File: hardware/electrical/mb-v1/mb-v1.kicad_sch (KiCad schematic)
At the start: 17 parts, among them SW1 SW_MEC_5E, SW2 SW_MEC_5E, SW3 SW_MEC_5E, SW5 SW_MEC_5E, U1 ATmega328P-A, U2 PCF8574T, Y1 Crystal_GND24

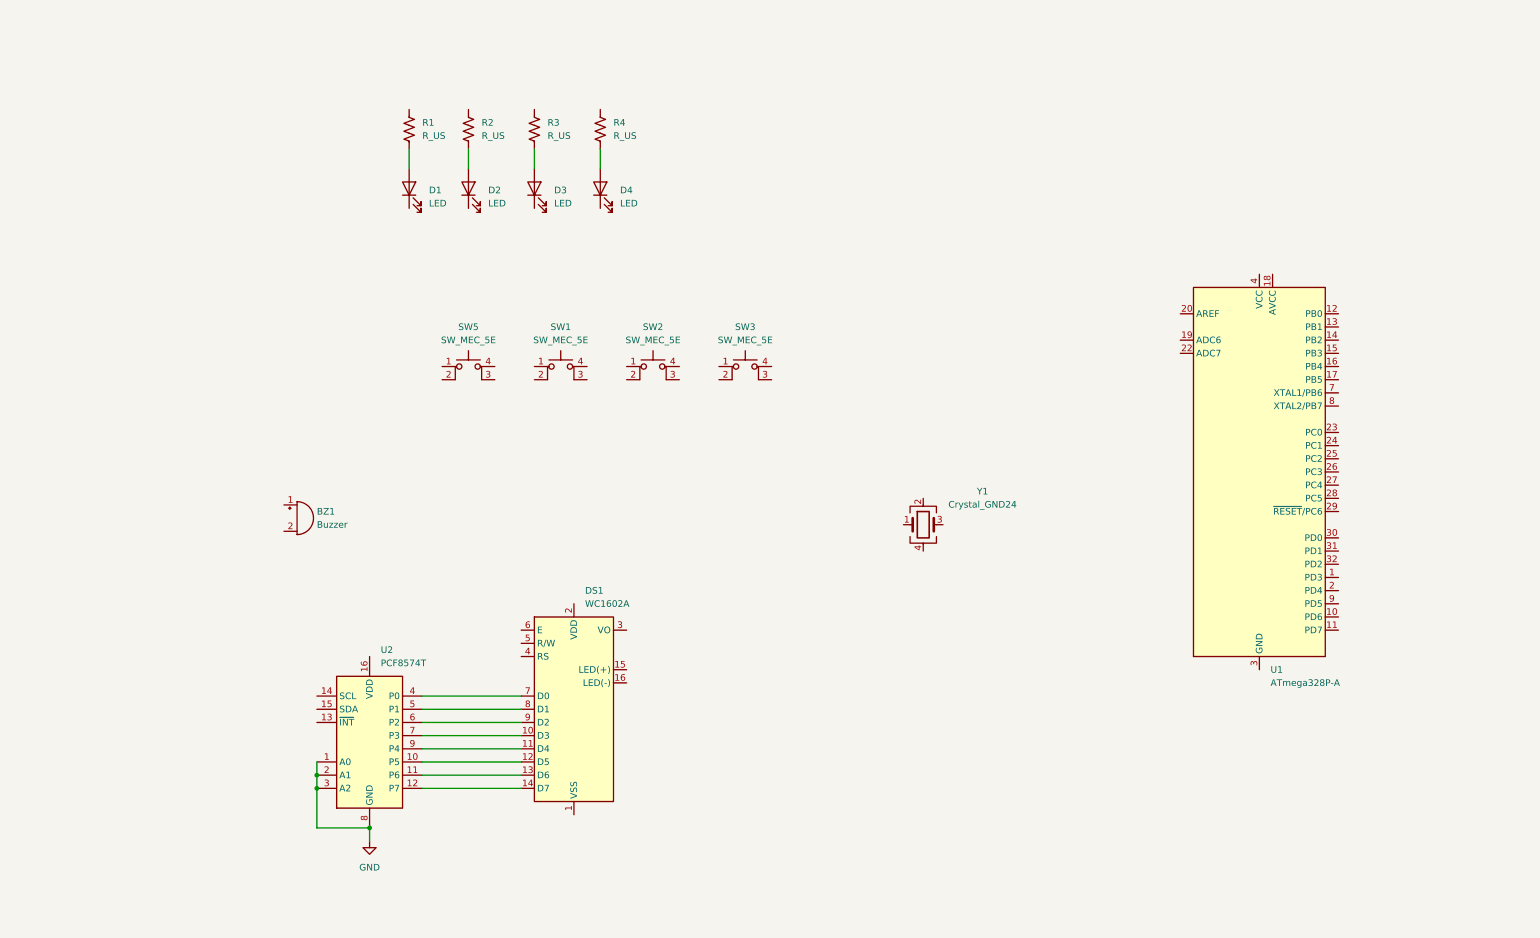
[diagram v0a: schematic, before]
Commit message: organize leds, buttons and buzzer
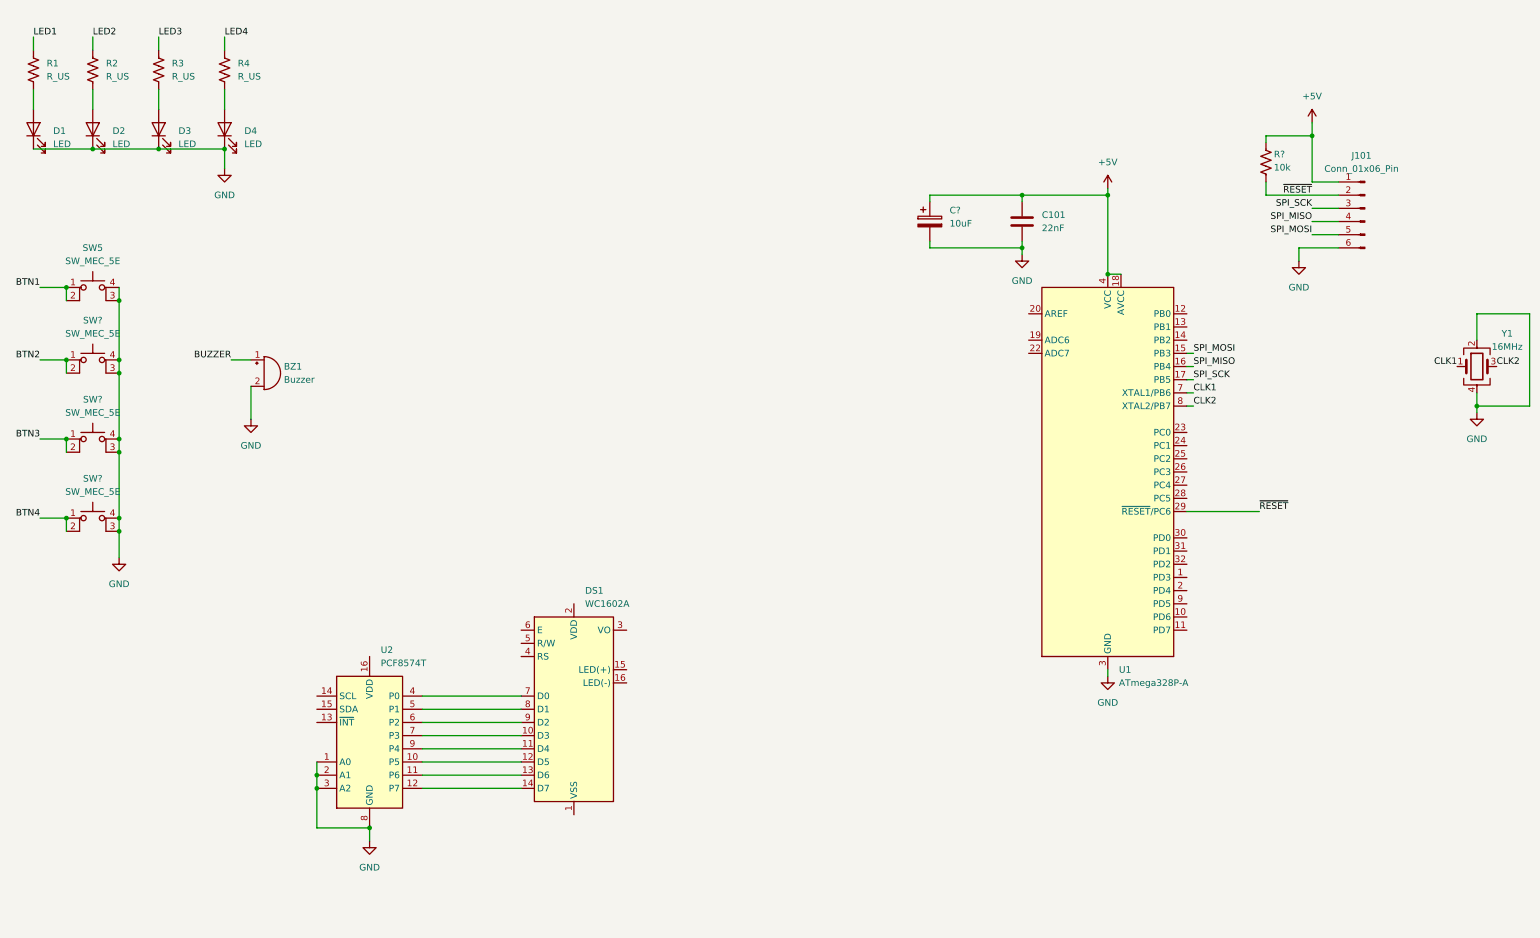
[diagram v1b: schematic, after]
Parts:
- removed SW1, SW2, SW3: SW_MEC_5E, symbol Switch:SW_MEC_5E
- added C101: 22nF, symbol Device:C
- added C?: 10uF, symbol Device:C_Polarized
- added J101: Conn_01x06_Pin, symbol Connector:Conn_01x06_Pin
- added R?: 10k, symbol Device:R_US
- added SW? (x3): SW_MEC_5E, symbol Switch:SW_MEC_5E
- Y1: value Crystal_GND24 -> 16MHz
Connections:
- net GND: now also BZ1.2 (-), D1.1 (K), D2.1 (K), D3.1 (K), D4.1 (K), SW5.3 (K), SW5.4 (A), U1.21 (GND), U1.3 (GND), U1.5 (GND), Y1.2, Y1.4, C101.2, C?.2, J101.6 (Pin_6), SW?.3 (K), SW?.3 (K), SW?.3 (K), SW?.4 (A), SW?.4 (A), SW?.4 (A)
- net SPI_MOSI: now reaches U1.15 (PB3)
- net SPI_MOSI: now also J101.5 (Pin_5)
- net SPI_MISO: now reaches U1.16 (PB4)
- net SPI_MISO: now also J101.4 (Pin_4)
- net SPI_SCK: now reaches U1.17 (PB5)
- net SPI_SCK: now also J101.3 (Pin_3)
- net +5V: now reaches U1.18 (AVCC)
- net +5V: now also U1.4 (VCC), U1.6 (VCC), C101.1, C?.1, J101.1 (Pin_1), R?.1
- net ~{RESET}: now reaches U1.29 (~{RESET}/PC6)
- net ~{RESET}: now also J101.2 (Pin_2), R?.2
- net CLK1: now reaches U1.7 (XTAL1/PB6)
- net CLK1: now also Y1.1
- net CLK2: now reaches U1.8 (XTAL2/PB7)
- net CLK2: now also Y1.3
- net LED1: now reaches R1.1
- net BUZZER: now reaches BZ1.1 (+)
- net LED4: now reaches R4.1
- net BTN1: now reaches SW5.1
- net BTN1: now also SW5.2
- net LED2: now reaches R2.1
- net LED3: now reaches R3.1
- new net BTN2: SW?.1, SW?.2
- new net BTN3: SW?.1, SW?.2
- new net BTN4: SW?.1, SW?.2
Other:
- moved on the sheet: BZ1, D1, D2, D3, D4, R1, R2, R3, R4, SW5, U1, Y1

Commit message: add usb and usb-serial converter
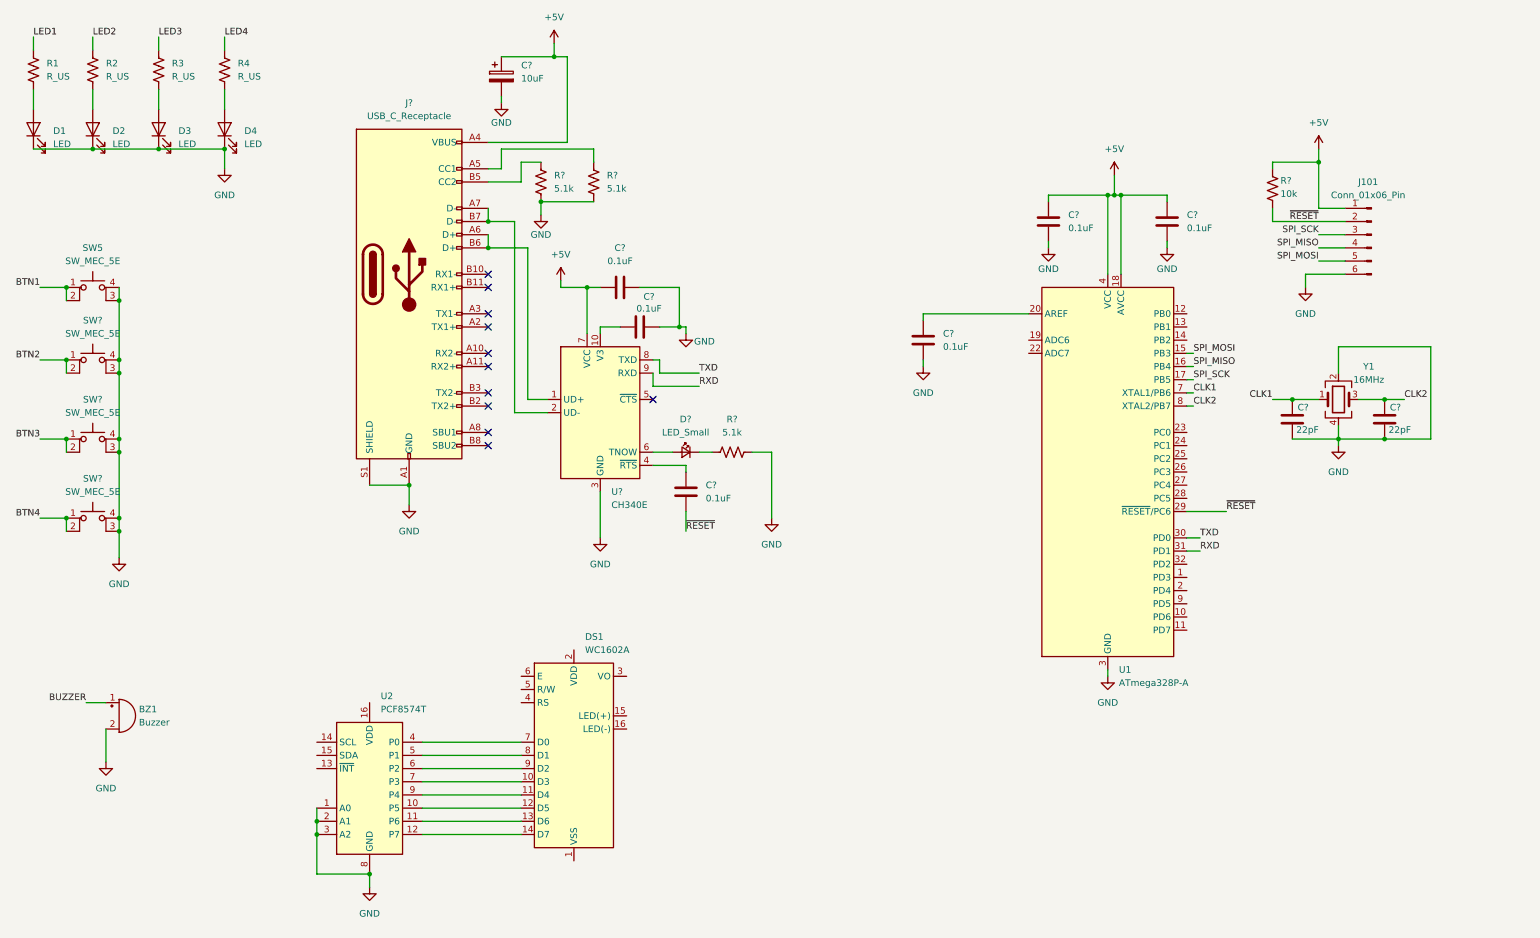
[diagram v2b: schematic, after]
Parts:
- removed C101: 22nF, symbol Device:C
- added C? (x2): 22pF, symbol Device:C
- added C? (x6): 0.1uF, symbol Device:C
- added D?: LED_Small, symbol Device:LED_Small
- added J?: USB_C_Receptacle, symbol Connector:USB_C_Receptacle
- added R? (x3): 5.1k, symbol Device:R_US
- added U?: CH340E, Package_SO:MSOP-10_3x3mm_P0.5mm, symbol Interface_USB:CH340E
- Y1: footprint (none) -> Crystal:Crystal_SMD_SeikoEpson_TSX3225-4Pin_3.2x2.5mm
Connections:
- net +5V: now also C?.1, C?.1, C?.1, J?.A4 (VBUS), J?.A9 (VBUS), J?.B4 (VBUS), J?.B9 (VBUS), U?.7 (VCC)
- net CLK1: now also C?.1
- net CLK2: now also C?.1
- net GND: now also C?.2, C?.2, C?.2, C?.2, C?.2, C?.2, C?.2, J?.A1 (GND), J?.A12 (GND), J?.B1 (GND), J?.B12 (GND), J?.S1 (SHIELD), R?.2, R?.2, R?.2, U?.3 (GND)
- net ~{RESET}: now also C?.2
- net at U1.20 (AREF): now also C?.1
- net TXD: now reaches U1.30 (PD0)
- net TXD: now also U?.8 (TXD)
- net RXD: now reaches U1.31 (PD1)
- net RXD: now also U?.9 (RXD)
- new net: J?.A6 (D+), J?.B6 (D+), U?.1 (UD+)
- new net: C?.1, U?.10 (V3)
- new net: J?.A7 (D-), J?.B7 (D-), U?.2 (UD-)
- new net: C?.1, U?.4 (~{RTS})
- new net: D?.2 (A), U?.6 (TNOW)
- new net: J?.A5 (CC1), R?.1
- new net: J?.B5 (CC2), R?.1
- new net: D?.1 (K), R?.1
- no-connect marks 0 -> 11
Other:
- moved on the sheet: BZ1, C?, DS1, J101, R?, U2, Y1

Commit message: complete placement and primary routing
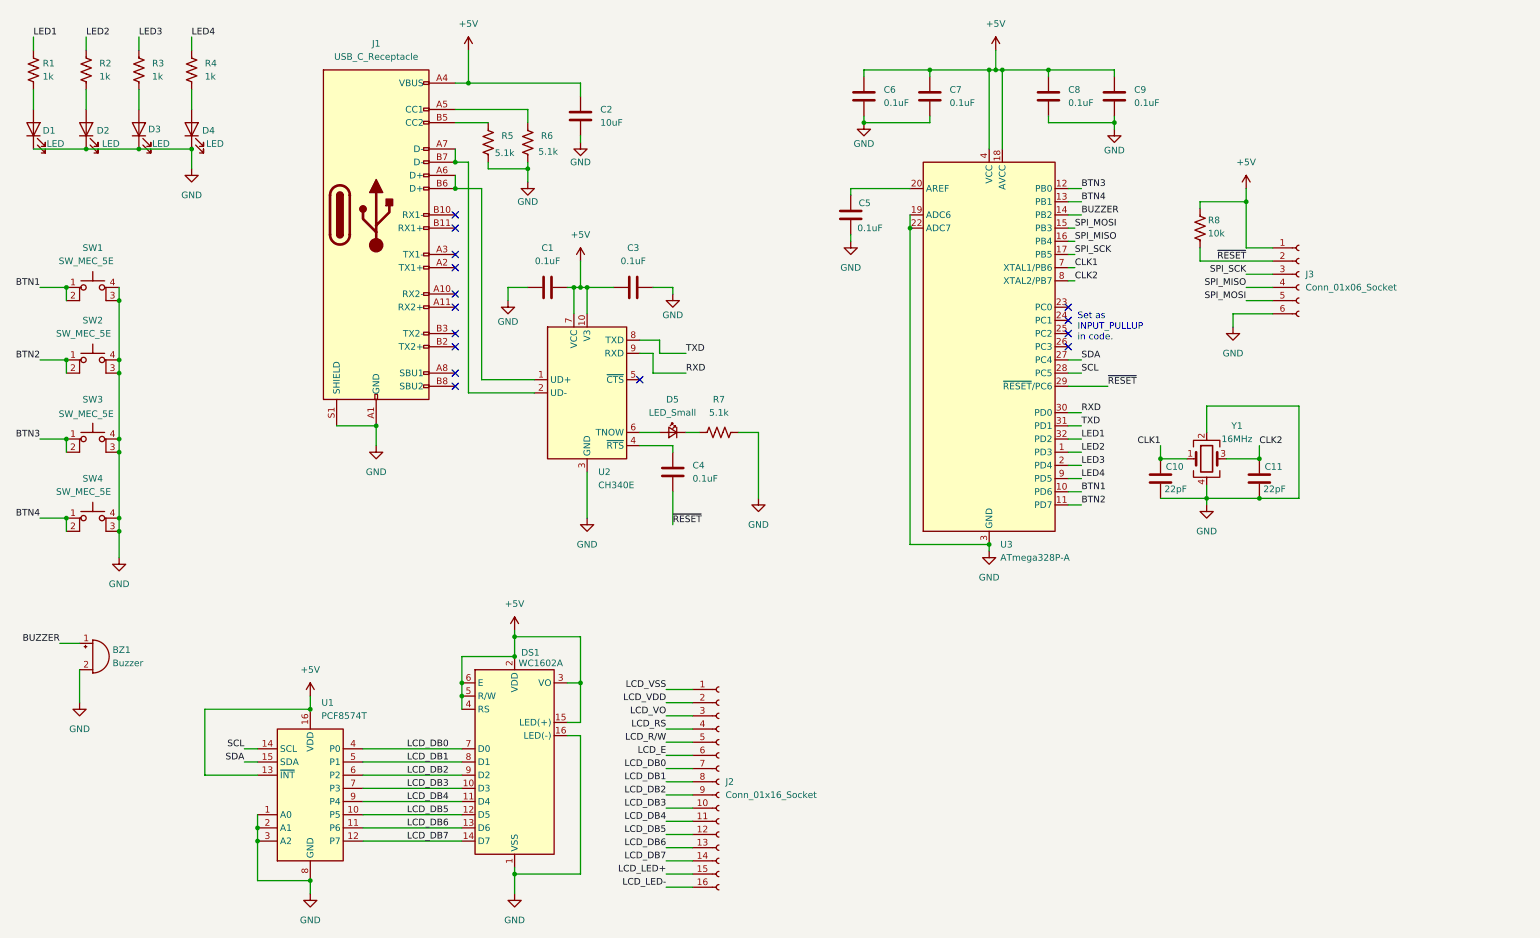
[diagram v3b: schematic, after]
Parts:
- removed C? (x2): 0.1uF, symbol Device:C
- removed C?: 10uF, symbol Device:C_Polarized
- removed J101: Conn_01x06_Pin, symbol Connector:Conn_01x06_Pin
- added C1, C3, C6, C9: 0.1uF, Capacitor_SMD:C_0603_1608Metric, symbol Device:C
- added C2: 10uF, Capacitor_SMD:C_0805_2012Metric, symbol Device:C
- added J2: Conn_01x16_Socket, symbol Connector:Conn_01x16_Socket
- added J3: Conn_01x06_Socket, symbol Connector:Conn_01x06_Socket
- C10, C11: renamed from C?; footprint (none) -> Capacitor_SMD:C_0402_1005Metric
- C4, C5, C7, C8: renamed from C?; footprint (none) -> Capacitor_SMD:C_0603_1608Metric
- J1: renamed from J?; footprint (none) -> Connector_USB:USB_C_Receptacle_Amphenol_12401548E4-2A
- R1, R2, R3, R4: value R_US -> 1k; footprint (none) -> Resistor_SMD:R_0603_1608Metric
- R5, R6, R7, R8: renamed from R?; footprint (none) -> Resistor_SMD:R_0603_1608Metric
- gave numbers to parts that had none: 5
- renumbered SW5 to SW1, U2 to U1, U1 to U3
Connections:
- net +5V: now also DS1.15 (LED(+)), DS1.2 (VDD), DS1.3 (VO), DS1.4 (RS), DS1.5 (R/W), DS1.6 (E), U1.13 (~{INT}), U1.16 (VDD), U2.10 (V3), C1.1, C2.1, C3.1, C6.1, C9.1, J3.1 (Pin_1)
- net BTN1: now also U3.10 (PD6)
- net BTN2: now also U3.11 (PD7)
- net BTN3: now also U3.12 (PB0)
- net BTN4: now also U3.13 (PB1)
- net BUZZER: now also U3.14 (PB2)
- net GND: now also DS1.1 (VSS), DS1.16 (LED(-)), U3.19 (ADC6), U3.22 (ADC7), C1.2, C2.2, C3.2, C6.2, C9.2, J3.6 (Pin_6)
- net LED1: now also U3.32 (PD2)
- net LED2: now also U3.1 (PD3)
- net LED3: now also U3.2 (PD4)
- net LED4: now also U3.9 (PD5)
- net RXD: now also U3.30 (PD0); no longer U3.31 (PD1)
- net SPI_MISO: now also J3.4 (Pin_4)
- net SPI_MOSI: now also J3.5 (Pin_5)
- net SPI_SCK: now also J3.3 (Pin_3)
- net TXD: now also U3.31 (PD1); no longer U3.30 (PD0)
- net ~{RESET}: now also J3.2 (Pin_2)
- net SDA: now reaches U3.27 (PC4)
- net SDA: now also U1.15 (SDA)
- net SCL: now reaches U3.28 (PC5)
- net SCL: now also U1.14 (SCL)
- net LCD_DB5: now reaches DS1.12 (D5), U1.10 (P5)
- net LCD_DB5: now also J2.12 (Pin_12)
- net LCD_DB6: now reaches DS1.13 (D6), U1.11 (P6)
- net LCD_DB6: now also J2.13 (Pin_13)
- net LCD_DB7: now reaches DS1.14 (D7), U1.12 (P7)
- net LCD_DB7: now also J2.14 (Pin_14)
- net LCD_DB0: now reaches DS1.7 (D0), U1.4 (P0)
- net LCD_DB0: now also J2.7 (Pin_7)
- net LCD_DB1: now reaches DS1.8 (D1), U1.5 (P1)
- net LCD_DB1: now also J2.8 (Pin_8)
- net LCD_DB2: now reaches DS1.9 (D2), U1.6 (P2)
- net LCD_DB2: now also J2.9 (Pin_9)
- net LCD_DB3: now reaches DS1.10 (D3), U1.7 (P3)
- net LCD_DB3: now also J2.10 (Pin_10)
- net LCD_DB4: now reaches DS1.11 (D4), U1.9 (P4)
- net LCD_DB4: now also J2.11 (Pin_11)
- new net LCD_E: J2.6 (Pin_6)
- new net LCD_LED+: J2.15 (Pin_15)
- new net LCD_LED-: J2.16 (Pin_16)
- new net LCD_RS: J2.4 (Pin_4)
- new net LCD_R/W: J2.5 (Pin_5)
- new net LCD_VDD: J2.2 (Pin_2)
- new net LCD_VO: J2.3 (Pin_3)
- new net LCD_VSS: J2.1 (Pin_1)
- no-connect marks 11 -> 15
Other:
- note added: "Set as INPUT_PULLUP in code."
- moved on the sheet: BZ1, C10, C11, C4, C5, C7, C8, D2, D3, D4, D5, DS1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

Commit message: replace usb symbol in schematic
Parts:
- added J?: TYPE-C-31-M-12, TYPE-C-31-M-12:HRO_TYPE-C-31-M-12, symbol TYPE-C-31-M-12:TYPE-C-31-M-12
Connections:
- net GND: now also J?.A1_B12 (GND), J?.B1_A12 (GND)
- new net: J?.S1 (SHIELD), J?.S2 (SHIELD), J?.S3 (SHIELD), J?.S4 (SHIELD)
- new net VBUS: J?.A4_B9 (VBUS), J?.B4_A9 (VBUS)
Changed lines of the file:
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@@
+	)
+	(symbol
+		(lib_id "TYPE-C-31-M-12:TYPE-C-31-M-12")
+		(at 77.47 125.73 0)
+		(unit 1)
+		(exclude_from_sim no)
+		(in_bom yes)
+		(on_board yes)
+		(dnp no)
+		(fields_autoplaced yes)
+		(property "Reference" "J?"
+			(at 77.47 107.95 0)
+			(effects
+				(font
+					(size 1.27 1.27)
+				)
+			)
+		)
+		(property "Value" "TYPE-C-31-M-12"
+			(at 77.47 110.49 0)
+			(effects
+				(font
+					(size 1.27 1.27)
+				)
+			)
+		)
+		(property "Footprint" "TYPE-C-31-M-12:HRO_TYPE-C-31-M-12"
+			(at 77.47 125.73 0)
+			(effects
+				(font
+					(size 1.27 1.27)
+				)
+				(justify bottom)
+				(hide yes)
+			)
+		)
+		(property "Datasheet" ""
+			(at 77.47 125.73 0)
+			(effects
+				(font
+					(size 1.27 1.27)
+				)
+				(hide yes)
+			)
+		)
+		(property "Description" ""
+			(at 77.47 125.73 0)
+			(effects
+				(font
+					(size 1.27 1.27)
+				)
+				(hide yes)
+			)
+		)
+		(property "MF" "HRO Electronics Co., Ltd."
+			(at 77.47 125.73 0)
+			(effects
+				(font
+					(size 1.27 1.27)
+				)
+				(justify bottom)
+				(hide yes)
+			)
+		)
+		(property "MAXIMUM_PACKAGE_HEIGHT" "3.26 mm"
+			(at 77.47 125.73 0)
+			(effects
+				(font
+					(size 1.27 1.27)
+				)
+				(justify bottom)
+				(hide yes)
+			)
+		)
+		(property "Package" "Package"
+			(at 77.47 125.73 0)
+			(effects
+				(font
+					(size 1.27 1.27)
+				)
+				(justify bottom)
+				(hide yes)
+			)
+		)
+		(property "Price" "None"
+			(at 77.47 125.73 0)
+			(effects
+				(font
+					(size 1.27 1.27)
+				)
+				(justify bottom)
+				(hide yes)
+			)
+		)
+		(property "Check_prices" "https://www.snapeda.com/parts/TYPE-C-31-M-12/HRO+Electronics+Co.%252C+Ltd./view-part/?ref=eda"
+			(at 77.47 125.73 0)
+			(effects
+				(font
+					(size 1.27 1.27)
+				)
+				(justify bottom)
+				(hide yes)
+			)
+		)
+		(property "STANDARD" "Manufacturer Recommendations"
+			(at 77.47 125.73 0)
+			(effects
+				(font
+					(size 1.27 1.27)
+				)
+				(justify bottom)
+				(hide yes)
+			)
+		)
+		(property "PARTREV" "2020.12.08"
+			(at 77.47 125.73 0)
+			(effects
+				(font
+					(size 1.27 1.27)
+				)
+				(justify bottom)
+				(hide yes)
+			)
+		)
+		(property "SnapEDA_Link" "https://www.snapeda.com/parts/TYPE-C-31-M-12/HRO+Electronics+Co.%252C+Ltd./view-part/?ref=snap"
+			(at 77.47 125.73 0)
+			(effects
+				(font
+					(size 1.27 1.27)
+				)
+				(justify bottom)
+				(hide yes)
+			)
+		)
+		(property "MP" "TYPE-C-31-M-12"
+			(at 77.47 125.73 0)
+			(effects
+				(font
+					(size 1.27 1.27)
+				)
+				(justify bottom)
+				(hide yes)
+			)
+		)
+		(property "Description_1" "USB Connectors 24 Receptacle 1 8.94*7.3mm RoHS"
+			(at 77.47 125.73 0)
+			(effects
+				(font
+					(size 1.27 1.27)
+				)
+				(justify bottom)
+				(hide yes)
+			)
+		)
+		(property "SNAPEDA_PN" "TYPE-C-31-M-12"
+			(at 77.47 125.73 0)
+			(effects
+				(font
+					(size 1.27 1.27)
+				)
+				(justify bottom)
+				(hide yes)
+			)
+		)
+		(property "Availability" "Not in stock"
+			(at 77.47 125.73 0)
+			(effects
+				(font
+					(size 1.27 1.27)
+				)
+				(justify bottom)
+				(hide yes)
+			)
+		)
+		(property "MANUFACTURER" "HRO Electronics Co., Ltd."
+			(at 77.47 125.73 0)
+			(effects
+				(font
+					(size 1.27 1.27)
+				)
+				(justify bottom)
+				(hide yes)
+			)
+		)
+		(pin "A6"
+		)
+		(pin "A7"
+		)
+		(pin "A8"
+		)
+		(pin "A4_B9"
+		)
+		(pin "B4_A9"
+		)
+		(pin "B8"
+		)
+		(pin "B7"
+		)
+		(pin "B6"
+		)
+		(pin "B5"
+		)
+		(pin "S1"
+		)
+		(pin "S2"
+		)
+		(pin "S3"
+		)
+		(pin "S4"
+		)
+		(pin "A1_B12"
+		)
+		(pin "B1_A12"
+		)
+		(pin "A5"
+		)
+		(instances
+			(project ""
+				(path "/10e9e845-0803-469c-b08a-573b4208af83"
+					(reference "J?")
+					(unit 1)
+				)
+			)
+		)
 	)
 	(symbol
